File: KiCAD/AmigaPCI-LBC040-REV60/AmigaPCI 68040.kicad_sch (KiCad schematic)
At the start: 0 parts

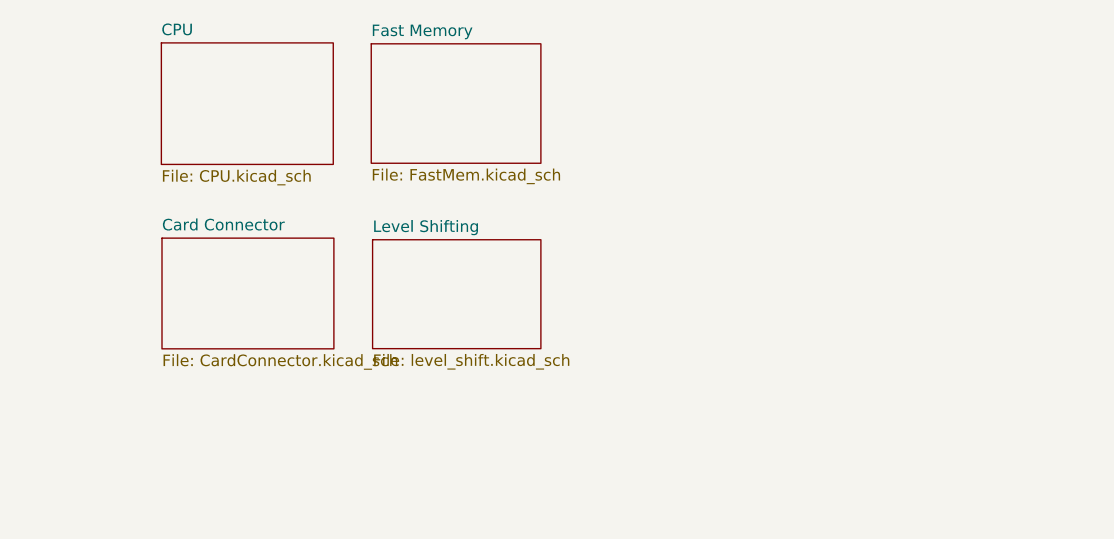
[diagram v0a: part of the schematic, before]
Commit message: Add part number for DIN41612 connector.
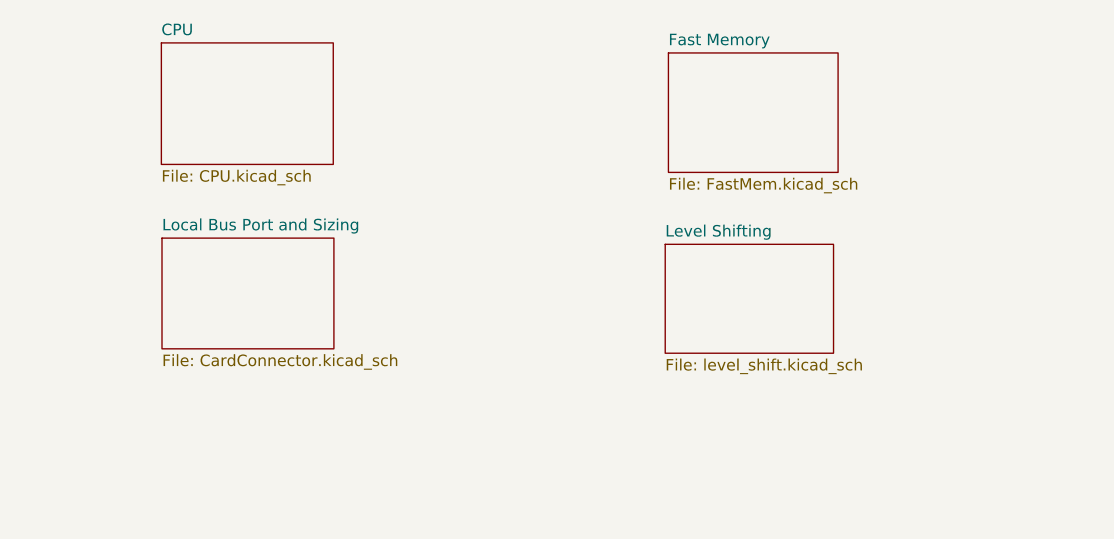
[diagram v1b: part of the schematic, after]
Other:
- sheet Card Connector renamed Local Bus Port and Sizing
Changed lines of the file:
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@@
 	)
 	(sheet
-		(at 56.8 54)
+		(at 89.312 54.508)
 		(size 18.7 12.1)
 		(fields_autoplaced yes)
@@
 		)
 		(property "Sheetname" "Level Shifting"
-			(at 56.8 53.2884 0)
+			(at 89.312 53.7964 0)
 			(effects
 				(font
@@
 		)
 		(property "Sheetfile" "level_shift.kicad_sch"
-			(at 56.8 66.6846 0)
+			(at 89.312 67.1926 0)
 			(effects
 				(font
@@
 	)
 	(sheet
-		(at 56.65 32.23)
+		(at 89.67 33.246)
 		(size 18.85 13.27)
 		(fields_autoplaced yes)
@@
 		)
 		(property "Sheetname" "Fast Memory"
-			(at 56.65 31.5184 0)
+			(at 89.67 32.5344 0)
 			(effects
 				(font
@@
 		)
 		(property "Sheetfile" "FastMem.kicad_sch"
-			(at 56.65 46.0846 0)
+			(at 89.67 47.1006 0)
 			(effects
 				(font
@@
 			(color 0 0 0 0.0000)
 		)
-		(property "Sheetname" "Card Connector"
+		(property "Sheetname" "Local Bus Port and Sizing"
 			(at 33.4 53.1084 0)
 			(effects
